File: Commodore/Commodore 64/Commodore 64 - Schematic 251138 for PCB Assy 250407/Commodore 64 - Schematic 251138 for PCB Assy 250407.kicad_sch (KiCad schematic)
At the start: 166 parts, among them CN1 KEYBOARD, CN2 USER PORT, CN3 CASSETTE, CN4 SERIAL BUS, CN5 AUDIO/VIDEO (8PIN FEMALE DIN), CN6 CARTRIDGE/EXPANSION (44PIN FE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, CN8 CONTROL PORT 2, CN9 CONTROL PORT 1, J99 RF_OUT, Q1 2SC1815, Q2 2SC1815, Q3 TP29B/2SD880, Q7 2SC1815, Q8 2SC1815, U1 6526_CIA_U1, U12,U24,U11,U23,U10,U22,U9,U21 4146_U9..U12,U21..U24, U13 74LS257_U13, U14 74LS258_U14, U15 74LS139_U15, U16 4066_U16, U17 872S100_PLA_U17, U18 6581_SID_U18, U19 6567_U19, U2 6526_CIA_U2, U20 LM556_U20, U25 74LS257_U25, U26 74LS373_U26, U27 74LS08, U28 4066, U29 74LS74_U29, U3 2364_BASIC_ROM_U3, U30 74LS193_U30, U31 74LS629N, U32 MC4044_U32, U4 2364_KERNAL_ROM_U4, U5 2332_CHAR_ROM_U5, U6 2114-30L_U6, U7 6510_MPU_U7, U8 7406, Y1 NOTE 2

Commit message: Some folder housekeeping
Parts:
- CN1: symbol Commodore_64:CONN_KEYBOARD_CN1 -> Commodore_64_Schematic_251138:CONN_KEYBOARD_CN1
- CN2: symbol Commodore_64:CONN_USER_CN2 -> Commodore_64_Schematic_251138:CONN_USER_CN2
- CN3: symbol Commodore_64:CONN_CASSETTE_CN3 -> Commodore_64_Schematic_251138:CONN_CASSETTE_CN3
- CN4: symbol Commodore_64:CONN_SERIAL_CN4 -> Commodore_64_Schematic_251138:CONN_SERIAL_CN4
- CN5: symbol Commodore_64:CONN_AV_CN5 -> Commodore_64_Schematic_251138:CONN_AV_CN5
- CN6: symbol Commodore_64:CONN_EXPANSION_CN6 -> Commodore_64_Schematic_251138:CONN_EXPANSION_CN6
- CN8: symbol Commodore_64:CONN_CTRL2_CN8 -> Commodore_64_Schematic_251138:CONN_CTRL2_CN8
- CN9: symbol Commodore_64:CONN_CTRL1_CN9 -> Commodore_64_Schematic_251138:CONN_CTRL1_CN9
- E1: symbol Commodore_64:JUMPER_SELECT -> Commodore_64_Schematic_251138:JUMPER_SELECT
- RF1: symbol Commodore_64:RF_MODULATOR -> Commodore_64_Schematic_251138:RF_MODULATOR
- RP1, RP2: symbol Commodore_64:RESISTOR_PACK_8PIN -> Commodore_64_Schematic_251138:RESISTOR_PACK_8PIN
- RP3: symbol Commodore_64:RESISTOR_PACK_8PIN_RN3 -> Commodore_64_Schematic_251138:RESISTOR_PACK_8PIN_RN3
- RP4: symbol Commodore_64:RESISTOR_PACK_10PIN_RN4 -> Commodore_64_Schematic_251138:RESISTOR_PACK_10PIN_RN4
- U1: symbol Commodore_64:6526_CIA_U1 -> Commodore_64_Schematic_251138:6526_CIA_U1
- U12,U24,U11,U23,U10,U22,U9,U21: symbol Commodore_64:4146_U9..U12,U21..U24 -> Commodore_64_Schematic_251138:4146_U9..U12,U21..U24
- U13: symbol Commodore_64:74LS257_U13 -> Commodore_64_Schematic_251138:74LS257_U13
- U14: symbol Commodore_64:74LS258_U14 -> Commodore_64_Schematic_251138:74LS258_U14
- U15: symbol Commodore_64:74LS139_U15 -> Commodore_64_Schematic_251138:74LS139_U15
- U16: symbol Commodore_64:4066_U16 -> Commodore_64_Schematic_251138:4066_U16
- U17: symbol Commodore_64:872S100_PLA_U17 -> Commodore_64_Schematic_251138:872S100_PLA_U17
- U18: symbol Commodore_64:6581_SID_U18 -> Commodore_64_Schematic_251138:6581_SID_U18
- U19: symbol Commodore_64:6567_U19 -> Commodore_64_Schematic_251138:6567_U19
- U2: symbol Commodore_64:6526_CIA_U2 -> Commodore_64_Schematic_251138:6526_CIA_U2
- U20: symbol Commodore_64:LM556_U20 -> Commodore_64_Schematic_251138:LM556_U20
- U25: symbol Commodore_64:74LS257_U25 -> Commodore_64_Schematic_251138:74LS257_U25
- U26: symbol Commodore_64:74LS373_U26 -> Commodore_64_Schematic_251138:74LS373_U26
- U27: symbol Commodore_64:74LS08_U27 -> Commodore_64_Schematic_251138:74LS08_U27
- U28: symbol Commodore_64:4066_U28 -> Commodore_64_Schematic_251138:4066_U28
- U29: symbol Commodore_64:74LS74_U29 -> Commodore_64_Schematic_251138:74LS74_U29
- U3: symbol Commodore_64:2364_BASIC_ROM_U3 -> Commodore_64_Schematic_251138:2364_BASIC_ROM_U3
- U30: symbol Commodore_64:74LS193_U30 -> Commodore_64_Schematic_251138:74LS193_U30
- U31: symbol Commodore_64:74LS629N_U31 -> Commodore_64_Schematic_251138:74LS629N_U31
- U32: symbol Commodore_64:MC4044_U32 -> Commodore_64_Schematic_251138:MC4044_U32
- U4: symbol Commodore_64:2364_KERNAL_ROM_U4 -> Commodore_64_Schematic_251138:2364_KERNAL_ROM_U4
- U5: symbol Commodore_64:2332_CHAR_ROM_U5 -> Commodore_64_Schematic_251138:2332_CHAR_ROM_U5
- U6: symbol Commodore_64:2114-30L_U6 -> Commodore_64_Schematic_251138:2114-30L_U6
- U7: symbol Commodore_64:6510_MPU_U7 -> Commodore_64_Schematic_251138:6510_MPU_U7
- U8: symbol Commodore_64:7406_U8 -> Commodore_64_Schematic_251138:7406_U8

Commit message: Completed C64 Schematic 251138.  Began working on RF Modulator.
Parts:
- added C100: .22, symbol Device:C_Small
- added C20, C21: .22 100V, symbol Device:C_Small
- added C200: .1 25V, symbol Device:C_Small
- added C44, C59 (x2), C66, C67, C89 (x2), C92, C98, C99: .1, symbol Device:C_Small
- added C57 (x2), C65: 10 25V, symbol Device:C_Polarized_Small
- added C88 (x2): 1000 25V, symbol Device:C_Polarized_Small
- added C9: 470 50V, symbol Device:C_Polarized_Small
- added C91: 100 16V, symbol Device:C_Polarized_Small
- added C97: .22 25V, symbol Device:C_Small
- added CN10: LED CONNECTOR, symbol Connector:Conn_01x03_Male
- added CN7: POWER INPUT, symbol Commodore_64_Schematic_251138:CONN_POWER_CN7
- added CR1: IN4371 2.7V, symbol Device:D_Zener
- added CR4: B40R, Diode_THT:Diode_Bridge_Round_D9.0mm, symbol Diode_Bridge:B40R
- added CR5, CR6: IN4001, symbol Device:D
- added D99: LED, symbol Device:LED
- added F1: 1A, symbol Device:Fuse
- added FB19, FB20, FB21: FerriteBead_Small, symbol Device:FerriteBead_Small
- added J100: LED, symbol Connector:Conn_01x02_Female
- added L2: 2.2µH, symbol Device:L
- added L4: L_Coupled, symbol Device:L_Coupled
- added L5: 1.2µH, symbol Device:L
- added N1: SHEET_1_NOTES, symbol Commodore_64_Schematic_251138:SHEET_1_NOTES
- added N?: SHEET_2_NOTES, symbol Commodore_64_Schematic_251138:SHEET_2_NOTES
- added R100: 1K, symbol Device:R_US
- added R37: 2.7K, symbol Device:R_US
- added R39: 390, symbol Device:R_US
- added R5: 560Ω, symbol Device:R_US
- added RF?: RF_MODULATOR, symbol Commodore_64_Schematic_251138:RF_MODULATOR
- added SW1: SW_DPST, symbol Switch:SW_DPST
- added unit 1 of U27
- added VR1: 7812, symbol Commodore_64_Schematic_251138:7812
- added VR2: 7805, symbol Commodore_64_Schematic_251138:7805
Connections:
- net +12V: now also C57.1, C59.1, VR1.2
- net +5V: now also C100.1, C44.2, C57.1, C59.1, C65.1, C66.2, C91.1, C92.1, CN7.4 (+5V), CN7.5 (+5V), L2.1, L5.1, R39.1, SW1.1, U27.1, U27.14, VR2.2
- net +9V: now also C88.1, C89.1, CR4.1 (+), CR6.2 (A), VR2.1
- net GND: now also C100.2, C200.2, C44.1, C57.2, C57.2, C59.2, C59.2, C65.2, C66.1, C67.1, C88.2, C88.2, C89.2, C89.2, C91.2, C92.2, C97.2, C98.2, C99.2, CN7.1 (GND), CN7.2 (GND), CN7.3 (GND), CR1.2 (A), CR4.3 (-), FB20.2, U27.7, VR1.3, VR2.3
- net VCC: now also C67.2, FB19.1
- net 60Hz: now reaches U1.19 (TOD), U2.19 (TOD)
- net 60Hz: now also R37.1, U27.3
- net 9VAC: now reaches CN2.10 (9VAC)
- net 9VAC: now also CN2.11 (9VAC), C20.1, C21.2, C9.2, C99.1, CN7.6 (9VAC), CN7.7 (9VAC), CR4.2, CR4.4, F1.1, L4.1, L4.4, R5.2, SW1.3
- new net: R100.1, R37.2, U27.2
- new net: C200.1, CR1.1 (K), R100.2, R5.1
- new net: D99.2 (A), J100.1 (Pin_1)
- new net: D99.1 (K), J100.2 (Pin_2)
- new net: C88.1, C89.1, CR5.1 (K), VR1.1
- new net: C9.1, CR5.2 (A), CR6.1 (K)
- new net: C20.2, L4.2, SW1.4
- new net: CN10.1 (Pin_1), CN10.3 (Pin_3), FB21.2
- new net: CN10.2 (Pin_2), FB20.1
- new net: FB21.1, R39.2
- new net: C21.1, C98.1, F1.2, L4.3
- new net: FB19.2, L2.2
- new net: C97.1, L5.2, SW1.2
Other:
- added sheet RF MODULATOR (Commodore 64 - RF Modulator for Schematic 2251138.kicad_sch)
- note added: "(7PIN MALE DIN)"
- note added: "SHEET 2"
- note added: "SHIELD GND"
- moved on the sheet: C10, C101, C105, C107, C108, C11, C12, C13, C14, C15, C16, C17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

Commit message: Completed C64 Schematic 251138
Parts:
- removed RF1, RF?: RF_MODULATOR, symbol Commodore_64_Schematic_251138:RF_MODULATOR
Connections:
- net RF MODULATOR/COLOR_{IN}: now also FB14.2
- net RF MODULATOR/COLOR_{OUT}: now also CN5.6 (COLOR)
- net RF MODULATOR/SYNC+LUM_{IN}: now also FB15.2
- net RF MODULATOR/AUDIO: now reaches C13.2, CN5.3 (AUD_OUT)
- net RF MODULATOR/COMP_{OUT}: now reaches CN5.4 (COMP_VID)
- net RF MODULATOR/SYNC+LUM_{OUT}: now reaches CN5.1 (LUM)
- net RF MODULATOR/ICS: now reaches E1.1 (A)
- net RF MODULATOR/RF_OUT: now reaches J99.1 (In)
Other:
- sheet RF MODULATOR ports: added +B, AUDIO, COMP_{OUT}, ICS, RF_OUT, SYNC+LUM_{OUT}; removed none

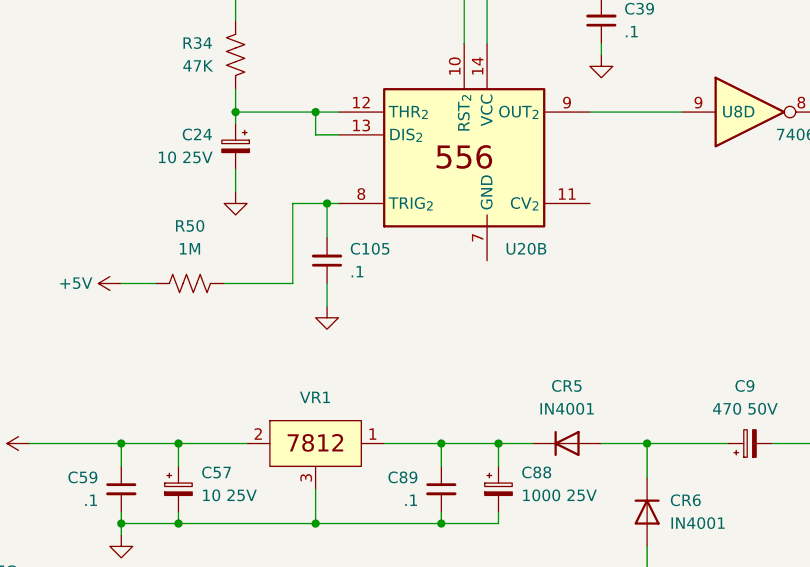
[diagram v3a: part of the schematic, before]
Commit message: Missed a ground connection on U20B - C64 251138
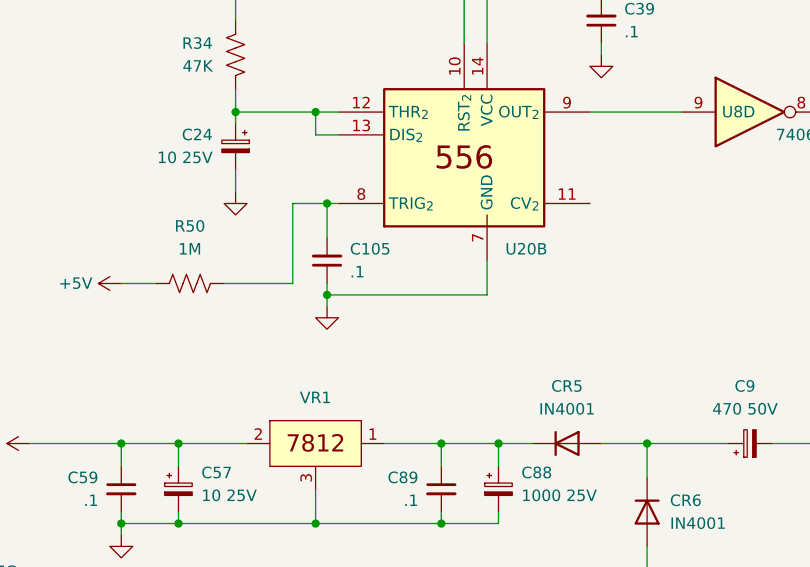
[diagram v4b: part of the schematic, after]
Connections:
- net GND: now also U20.7 (GND)
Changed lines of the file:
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@@
   (junction (at 292.1 951.23) (diameter 0) (color 0 0 0 0)
   )
+  (junction (at 603.25 999.49) (diameter 0) (color 0 0 0 0)
+  )
   (junction (at 259.08 937.26) (diameter 0) (color 0 0 0 0)
   )
@@
     (stroke (width 0) (type default) (color 0 0 0 0))
   )
+  (wire (pts (xy 603.25 999.49) (xy 603.25 998.22))
+    (stroke (width 0) (type default) (color 0 0 0 0))
+  )
   (wire (pts (xy 426.72 735.33) (xy 426.72 737.87))
     (stroke (width 0) (type default) (color 0 0 0 0))
@@
     (stroke (width 0) (type default) (color 0 0 0 0))
   )
-  (wire (pts (xy 603.25 1000.76) (xy 603.25 998.22))
+  (wire (pts (xy 603.25 1000.76) (xy 603.25 999.49))
     (stroke (width 0) (type default) (color 0 0 0 0))
   )
@@
     (stroke (width 0) (type default) (color 0 0 0 0))
   )
+  (wire (pts (xy 621.03 999.49) (xy 603.25 999.49))
+    (stroke (width 0) (type default) (color 0 0 0 0))
+  )
   (wire (pts (xy 718.82 864.87) (xy 718.82 868.68))
     (stroke (width 0) (type default) (color 0 0 0 0))
@@
     (stroke (width 0) (type default) (color 0 0 0 0))
   )
+  (wire (pts (xy 621.03 995.68) (xy 621.03 999.49))
+    (stroke (width 0) (type default) (color 0 0 0 0))
+  )
